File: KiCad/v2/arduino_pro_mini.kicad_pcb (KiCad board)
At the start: 4 copper layers, 24 x 39.2 mm, 35 parts, among them IC101 ATMEGA328P-AU, J101 Conn_01x06_Pin, J102 Conn_01x15_Pin, J103 Conn_01x15_Pin, SW101 SW_Omron_B3FS, U101 SPX3819M5-L-5-0/TR, U102 SPX3819M5-L-3-3/TR, Y101 16Mhz

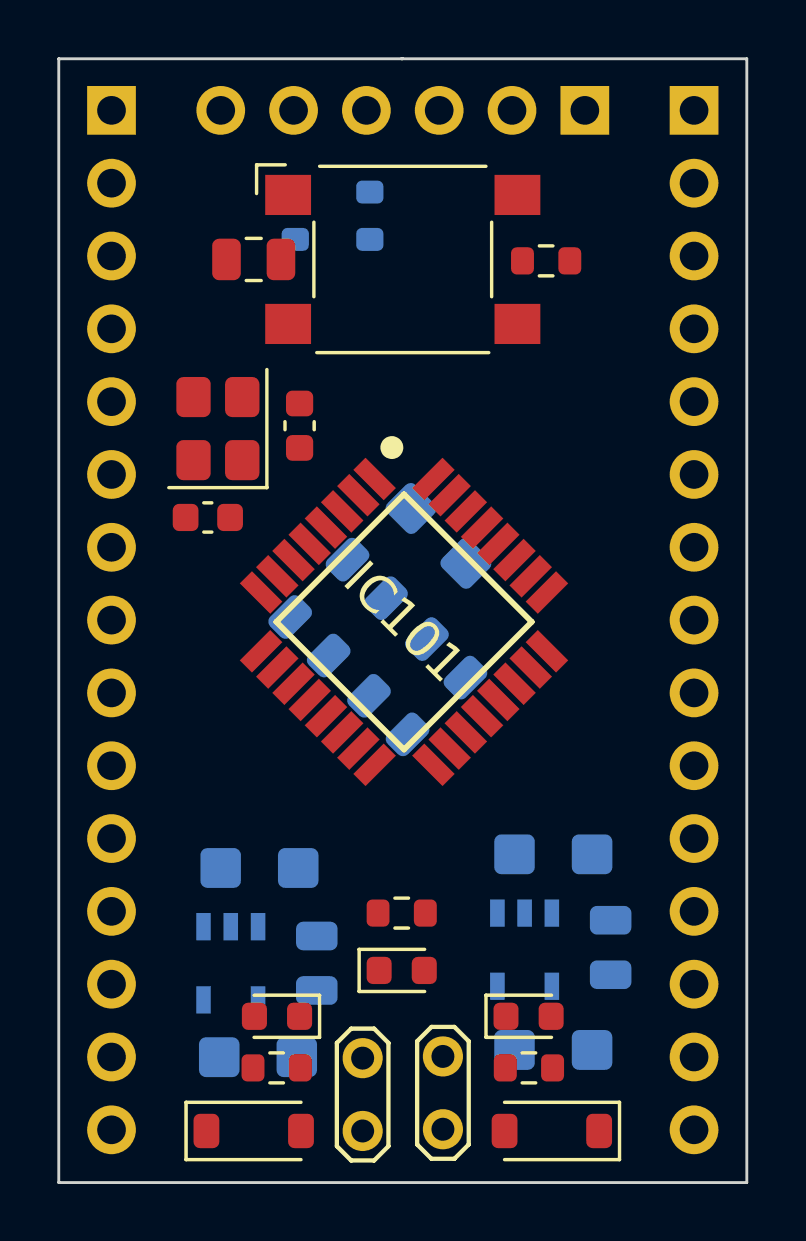
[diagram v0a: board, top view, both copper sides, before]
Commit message: Initial signal routing
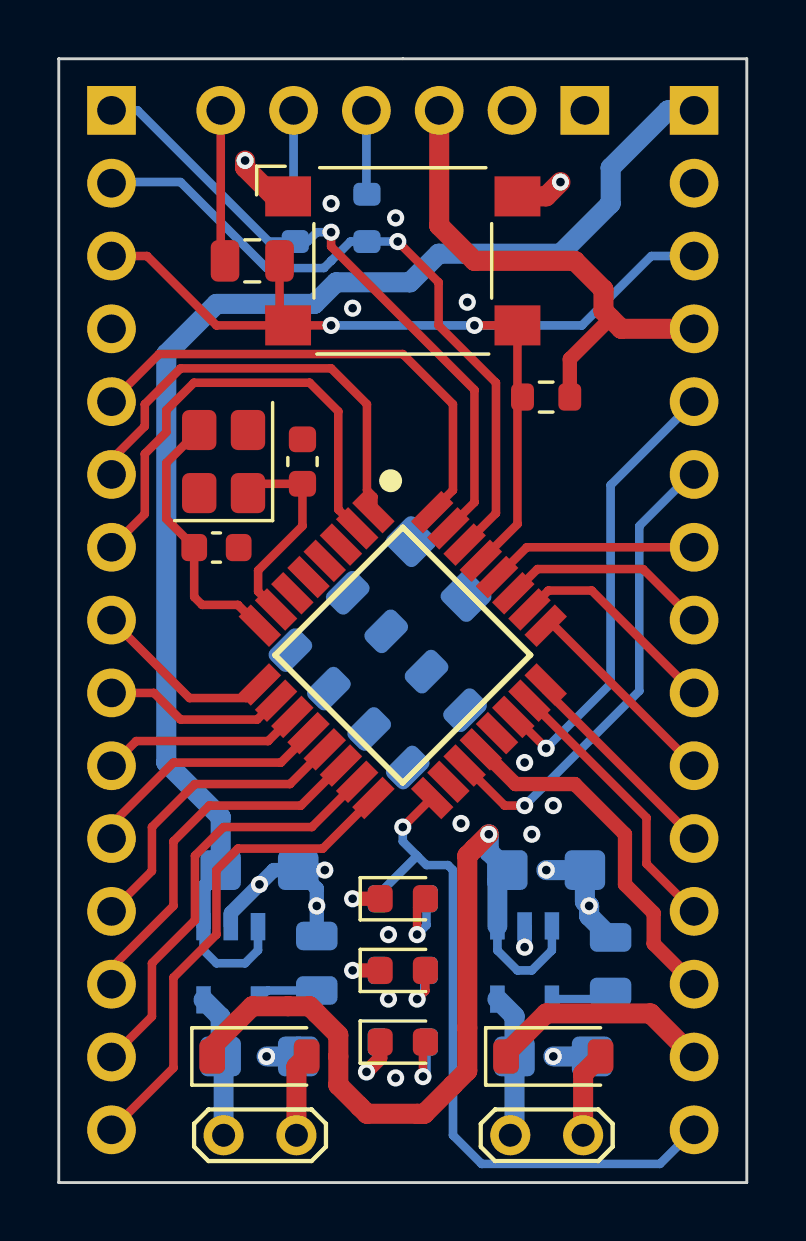
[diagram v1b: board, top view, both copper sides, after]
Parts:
- R101, R103, R104: moved to B.Cu
- moved R103 5.56 mm to (50.0, 80.0)
- moved JP101 5.55 mm to (43.8, 85.8), turned to 0 degrees
- moved R102 4.75 mm to (55.0, 60.0)
- moved D104 4.67 mm to (50.0, 80.0)
- moved R101 4.49 mm to (50.0, 82.5), turned to 0 degrees
- moved D102 4.48 mm to (50.0, 82.5), turned to 0 degrees
- moved JP102 3.62 mm to (53.8, 85.8), turned to 0 degrees
- moved D101 2.61 mm to (45.0, 83.0)
- moved D103 2.60 mm to (55.2, 83.0), turned to 0 degrees
- moved D105 2.50 mm to (50.0, 77.5)
- moved C108 1.25 mm to (46.5, 62.2)
- moved Y101 1.17 mm to (43.8, 62.2)
- moved IC101 1.16 mm to (50.0, 69.0)
- moved C101 1.16 mm to (51.2, 66.0)
- moved C102 1.16 mm to (46.8, 69.5)
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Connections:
- D105 pad 1: Net-(D105-K) -> GND
- D105 pad 2: D13_SCK -> Net-(D105-A)
- R101 pad 1: +5V_LDO -> +5V
- R103 pad 1: +3V3_LDO -> +3V3
- R104 pad 1: Net-(D105-K) -> D13_SCK
- R104 pad 2: GND -> Net-(D105-A)
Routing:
- net VIN: track 0.00 -> 47.6 mm
- net +5V: track 0.00 -> 47.6 mm, vias 0 -> 1
- net RESET: track 0.00 -> 35.9 mm, vias 0 -> 2
- net D13_SCK: track 0.00 -> 24.7 mm, vias 0 -> 1
- net D0_RX: track 0.00 -> 24.1 mm, vias 0 -> 1
- net D1_TX: track 0.00 -> 22.5 mm, vias 0 -> 1
- net GND: track 0.00 -> 21.6 mm, vias 0 -> 24
- net D2: track 0.00 -> 17.4 mm
- net D12_MISO: track 0.00 -> 17.1 mm
- net D4: track 0.00 -> 16.7 mm
- net A6: track 0.00 -> 16.7 mm, vias 0 -> 1
- net A7: track 0.00 -> 15.8 mm, vias 0 -> 1
- net D3: track 0.00 -> 15.6 mm
- net D11_MOSI: track 0.00 -> 15.0 mm
- net D10: track 0.00 -> 12.8 mm
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
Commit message: Power signals routing
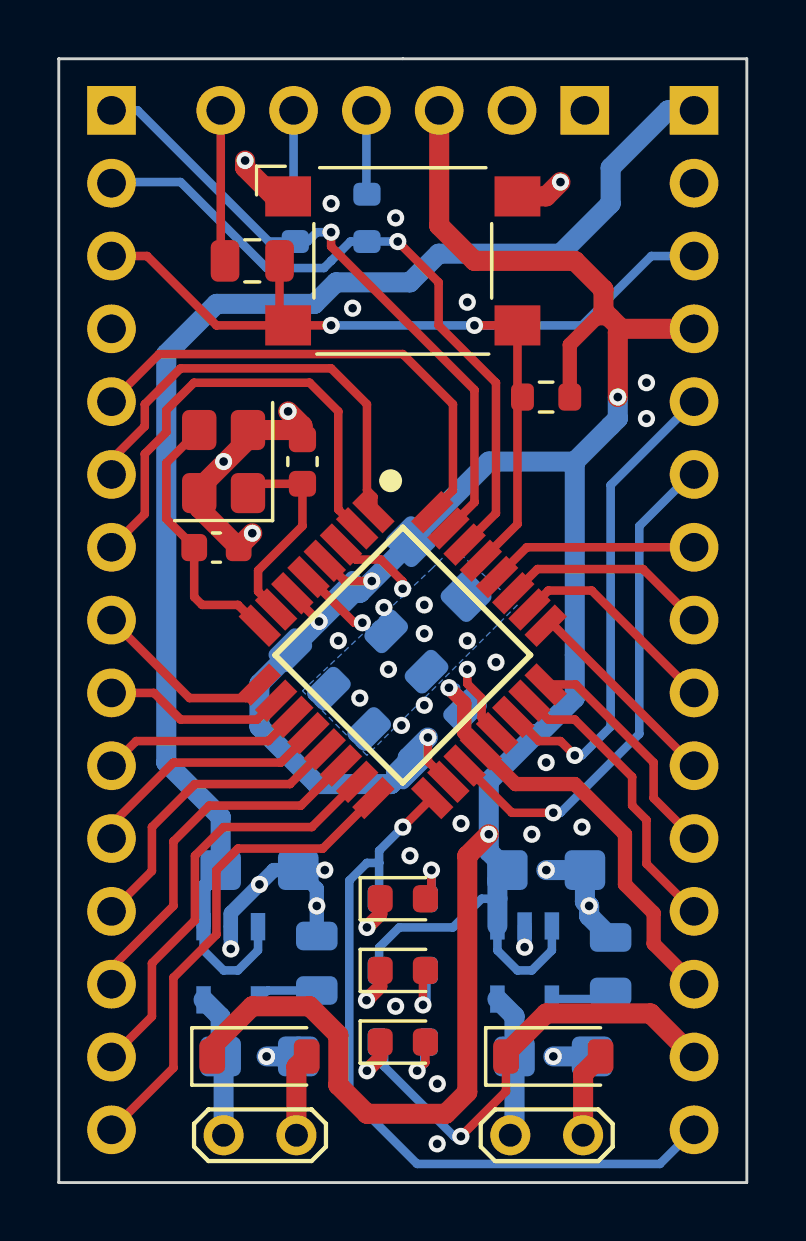
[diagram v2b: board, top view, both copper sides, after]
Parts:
- moved D102 2.50 mm to (50.0, 80.0)
- moved D104 2.50 mm to (50.0, 82.5)
- moved R101 2.50 mm to (50.0, 80.0)
- moved R103 2.50 mm to (50.0, 82.5)
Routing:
- net +5V: track 47.6 -> 102.2 mm, vias 1 -> 5
- net GND: track 21.6 -> 40.2 mm, vias 24 -> 44
- net +3V3: track 8.30 -> 16.4 mm, vias 0 -> 1
- net AREF: track 12.5 -> 16.4 mm, vias 0 -> 1
- net D13_SCK: track 24.7 -> 26.6 mm
- net A1: track 7.52 -> 8.62 mm
- net A7: track 15.8 -> 16.9 mm
- net A6: track 16.7 -> 17.8 mm
- net Net-(D105-A): track 2.75 -> 2.16 mm
- net A0: track 9.73 -> 10.3 mm
- added copper zone on B.Cu, net GND

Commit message: sulk screen updates
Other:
- board text added: "16 Mhz"
- board text added: "328P-AU"
- board text added: "3V3"
- board text added: "5V"
- board text added: "A0"
- board text added: "A1"
- board text added: "A2"
- board text added: "A3"
- board text added: "A4"
- board text added: "A5"
- board text added: "A6"
- board text added: "A7"
- board text added: "AREF"
- board text added: "ATMEGA"
- board text added: "D0"
- board text added: "D1"
- board text added: "D10"
- board text added: "D11"
- board text added: "D12"
- board text added: "D13"
- board text added: "D2/D3"
- board text added: "D4 D5"
- board text added: "D6"
- board text added: "D7"
- board text added: "D8"
- board text added: "D9"
- board text added: "DTR"
- board text added: "G"
- board text added: "RST"
- board text added: "RXD"
- board text added: "TXD"
- board text added: "VIN"

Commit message: DCR fix
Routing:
- net Net-(D104-A): track 2.25 -> 3.46 mm
- net +3V3: track 16.4 -> 17.2 mm
- net D13_SCK: track 26.6 -> 27.2 mm
- net GND: track 40.2 -> 40.5 mm, vias 44 -> 43
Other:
- board text added: "Jumpers"

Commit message: DCR fix
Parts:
- moved C108 0.39 mm to (46.5, 62.6)
- moved C109 0.39 mm to (43.5, 65.6)
- moved Y101 0.39 mm to (43.8, 62.6)
- moved JP101 0.25 mm to (43.8, 85.5)
- moved JP102 0.25 mm to (53.8, 85.5)
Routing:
- net XTAL_OUT: track 9.68 -> 8.58 mm
- net GND: vias 43 -> 48

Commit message: Power signals routing
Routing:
- net +5V: track 102.2 -> 103.9 mm
- net GND: track 40.5 -> 41.8 mm, vias 48 -> 44
- added copper zone on F.Cu, net GND

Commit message: JLCPCB rule check
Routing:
- net AREF: track 16.1 -> 18.1 mm
- net A6: track 17.8 -> 19.3 mm
- net A7: track 16.9 -> 18.0 mm
- net GND: track 41.8 -> 40.8 mm
- net D13_SCK: track 27.2 -> 27.8 mm
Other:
- board text added: "16 Mhz 5V"
- board text added: "328P"
- board text added: "AU"
- board text removed: "16 Mhz"
- board text removed: "328P-AU"
